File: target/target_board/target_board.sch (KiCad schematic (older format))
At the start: 72 parts, among them J1 USB_B_Micro, J2 SPI_CONN, J3 UART_CONN, J4 I2C_CONN, J5 SWD_CONN, J6 DFU, Q1 RZM001P02, Q2 RZM001P02, SW1 SW_Push, SW10 SW_Push, SW11 SW_Push, SW12 SW_Push, SW13 SW_Push, SW2 SW_Push, SW3 SW_Push, SW4 SW_Push, SW5 SW_Push, SW6 SW_Push, SW7 SW_Push, SW8 SW_Push, SW9 SW_Push, U1 25LCxxx, U2 AP2112K-3.3, U3 STM32F072C8Tx, U4 24LC04, U5 VDMX10.0, U6 VDMX10.0, U7 VDMX10.0, U8 VDMX10.0, U9 MCP23017_SS

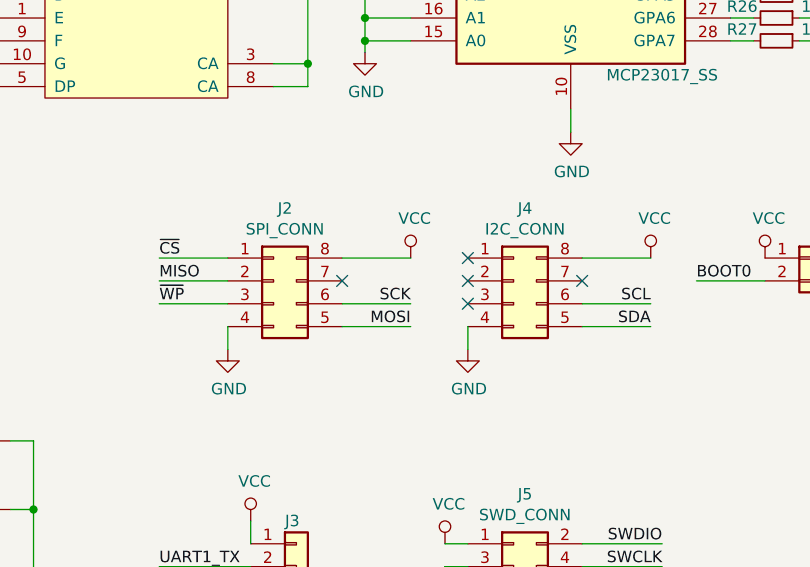
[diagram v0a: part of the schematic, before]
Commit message: Rough layout of components for target.
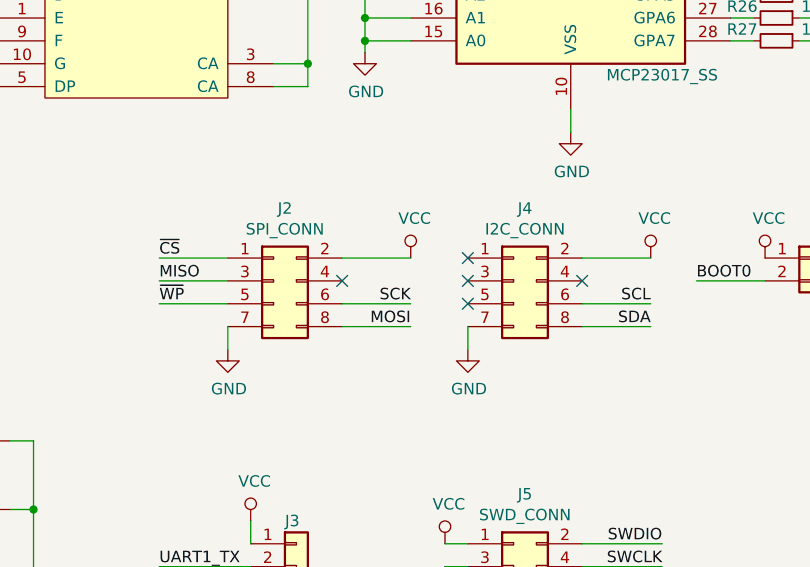
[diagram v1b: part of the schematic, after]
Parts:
- removed J2: SPI_CONN, symbol Connector_Generic:Conn_02x04_Counter_Clockwise
- removed J4: I2C_CONN, symbol Connector_Generic:Conn_02x04_Counter_Clockwise
- added J2: SPI_CONN, Connector_PinHeader_2.54mm:PinHeader_2x04_P2.54mm_Vertical, symbol Connector_Generic:Conn_02x04_Odd_Even
- added J4: I2C_CONN, Connector_PinHeader_2.54mm:PinHeader_2x04_P2.54mm_Vertical, symbol Connector_Generic:Conn_02x04_Odd_Even
- C1, C10, C11, C12, C2, C3, C4, C5, C6, C7, C8, C9: footprint (none) -> Capacitor_SMD:C_0603_1608Metric
- D1, D2, D3: footprint (none) -> LED_SMD:LED_0603_1608Metric_Castellated
- J1: footprint (none) -> Connector_USB:USB_Micro-B_Amphenol_10103594-0001LF_Horizontal
- J3: footprint (none) -> Connector_PinHeader_2.54mm:PinHeader_1x05_P2.54mm_Vertical
- J5: footprint (none) -> Connector_PinHeader_1.27mm:PinHeader_2x05_P1.27mm_Vertical
- J6: footprint (none) -> Connector_PinHeader_2.54mm:PinHeader_1x02_P2.54mm_Vertical
- Q1, Q2: footprint (none) -> Package_TO_SOT_SMD:SOT-723
- R1, R10, R11, R12, R13, R14, R15, R16, R17, R18, R19, R2, R20, R21, R22, R23, R24, R25, R26, R27, R3, R4, R5, R6, R7, R8, R9: footprint (none) -> Resistor_SMD:R_0603_1608Metric
- SW1, SW10, SW11, SW12, SW13, SW2, SW3, SW4, SW5, SW6, SW7, SW8, SW9: footprint (none) -> Button_Switch_SMD:SW_SPST_PTS645
- U1, U4: footprint (none) -> Package_SO:SOIC-8_3.9x4.9mm_P1.27mm
- U5, U6, U7, U8: footprint (none) -> Matir:VDMX10.0
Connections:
- net GND: now also J2.7 (Pin_7), J4.7 (Pin_7)
- net MISO: now also J2.3 (Pin_3)
- net MOSI: now also J2.8 (Pin_8)
- net SCK: now also J2.6 (Pin_6)
- net SCL: now also J4.6 (Pin_6)
- net SDA: now also J4.8 (Pin_8)
- net VCC: now also J2.2 (Pin_2), J4.2 (Pin_2)
- net ~CS: now also J2.1 (Pin_1)
- net ~WP: now also J2.5 (Pin_5)

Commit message: Continue layout
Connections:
- net COL1: now also U3.11 (PA1); no longer U3.45 (PB8)
- net COL2: now also U3.10 (PA0); no longer U3.46 (PB9)
- net DISPA: now also U3.13 (PA3); no longer U3.40 (PB4)
- net DISPB: now also U3.22 (PB11); no longer U3.41 (PB5)
- net LED_G: now also U3.46 (PB9); no longer U3.10 (PA0)
- net LED_R: now also U3.39 (PB3); no longer U3.12 (PA2)
- net LED_Y: now also U3.45 (PB8); no longer U3.11 (PA1)
- net ROW4: now also U3.12 (PA2); no longer U3.39 (PB3)
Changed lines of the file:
@@
 Wire Wire Line
 	3300 4350 3800 4350
-Text Label 3800 4150 2    50   ~ 0
+Text Label 1550 5050 0    50   ~ 0
 LED_G
-Text Label 3800 4250 2    50   ~ 0
+Text Label 1550 4950 0    50   ~ 0
 LED_Y
-Text Label 3800 4350 2    50   ~ 0
+Text Label 1550 4450 0    50   ~ 0
 LED_R
 Wire Wire Line
@@
 NoConn ~ 3300 4950
 NoConn ~ 3300 5650
-NoConn ~ 3300 4450
 Wire Wire Line
 	1550 4750 2000 4750
@@
 Text Label 1550 4350 0    50   ~ 0
 ROW3
-Text Label 1550 4450 0    50   ~ 0
+Text Label 3800 4350 2    50   ~ 0
 ROW4
-Text Label 1550 4950 0    50   ~ 0
+Text Label 3800 4250 2    50   ~ 0
 COL1
-Text Label 1550 5050 0    50   ~ 0
+Text Label 3800 4150 2    50   ~ 0
 COL2
 Text Label 1550 5150 0    50   ~ 0
 COL3
-NoConn ~ 2000 5250
 NoConn ~ 2000 5350
 NoConn ~ 2000 5450
@@
 Text Label 3800 5350 2    50   ~ 0
 USB_P
-Wire Wire Line
-	2000 4550 1550 4550
-Wire Wire Line
-	2000 4650 1550 4650
-Text Label 1550 4550 0    50   ~ 0
+Text Label 3800 4450 2    50   ~ 0
 DISPA
-Text Label 1550 4650 0    50   ~ 0
+Text Label 1550 5250 0    50   ~ 0
 DISPB
 $Comp
@@
 	1    0    0    -1
 $EndComp
+Wire Wire Line
+	3800 4450 3300 4450
+NoConn ~ 2000 4550
+Wire Wire Line
+	2000 5250 1550 5250
+NoConn ~ 2000 4650
 $EndSCHEMATC

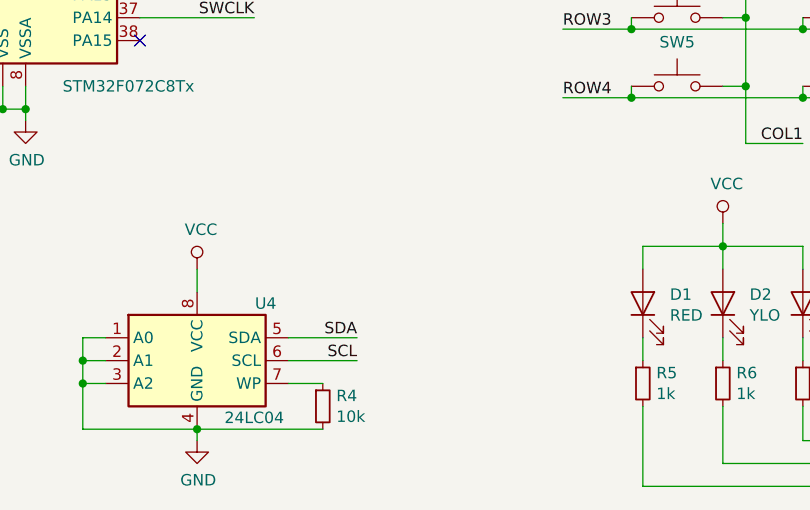
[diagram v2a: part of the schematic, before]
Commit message: Add missing I2C pullups
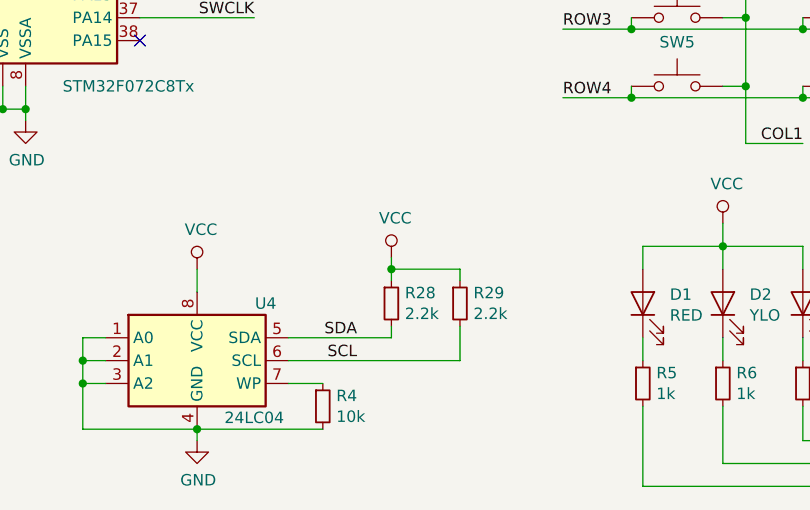
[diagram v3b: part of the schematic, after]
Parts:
- added R28, R29: 2.2k, Resistor_SMD:R_0603_1608Metric, symbol Device:R_Small
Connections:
- net SCL: now also R29.2
- net SDA: now also R28.2
- net VCC: now also R28.1, R29.1
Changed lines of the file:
@@
 Wire Wire Line
 	10600 3200 10500 3200
-Wire Wire Line
-	3950 6950 4250 6950
-Wire Wire Line
-	3950 7050 4250 7050
 Text Label 4250 6950 2    50   ~ 0
 SDA
@@
 	2000 5250 1550 5250
 NoConn ~ 2000 4650
+$Comp
+L power:VCC #PWR030
+U 1 1 5EBEFE5F
+P 4400 6600
+F 0 "#PWR030" H 4400 6450 50  0001 C CNN
+F 1 "VCC" H 4417 6773 50  0000 C CNN
+F 2 "" H 4400 6600 50  0001 C CNN
+F 3 "" H 4400 6600 50  0001 C CNN
+	1    4400 6600
+	1    0    0    -1
+$EndComp
+$Comp
+L Device:R_Small R28
+U 1 1 5EBF090B
+P 4400 6800
+F 0 "R28" H 4459 6846 50  0000 L CNN
+F 1 "2.2k" H 4459 6755 50  0000 L CNN
+F 2 "Resistor_SMD:R_0603_1608Metric" H 4400 6800 50  0001 C CNN
+F 3 "~" H 4400 6800 50  0001 C CNN
+	1    4400 6800
+	1    0    0    -1
+$EndComp
+$Comp
+L Device:R_Small R29
+U 1 1 5EBF0DE2
+P 4700 6800
+F 0 "R29" H 4759 6846 50  0000 L CNN
+F 1 "2.2k" H 4759 6755 50  0000 L CNN
+F 2 "Resistor_SMD:R_0603_1608Metric" H 4700 6800 50  0001 C CNN
+F 3 "~" H 4700 6800 50  0001 C CNN
+	1    4700 6800
+	1    0    0    -1
+$EndComp
+Wire Wire Line
+	4400 6600 4400 6650
+Wire Wire Line
+	4400 6900 4400 6950
+Wire Wire Line
+	3950 6950 4400 6950
+Wire Wire Line
+	4700 7050 4700 6900
+Wire Wire Line
+	3950 7050 4700 7050
+Wire Wire Line
+	4700 6700 4700 6650
+Wire Wire Line
+	4700 6650 4400 6650
+Connection ~ 4400 6650
+Wire Wire Line
+	4400 6650 4400 6700
 $EndSCHEMATC
